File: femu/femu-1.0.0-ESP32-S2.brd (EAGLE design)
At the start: 24.1 x 15.8 mm, 44 parts

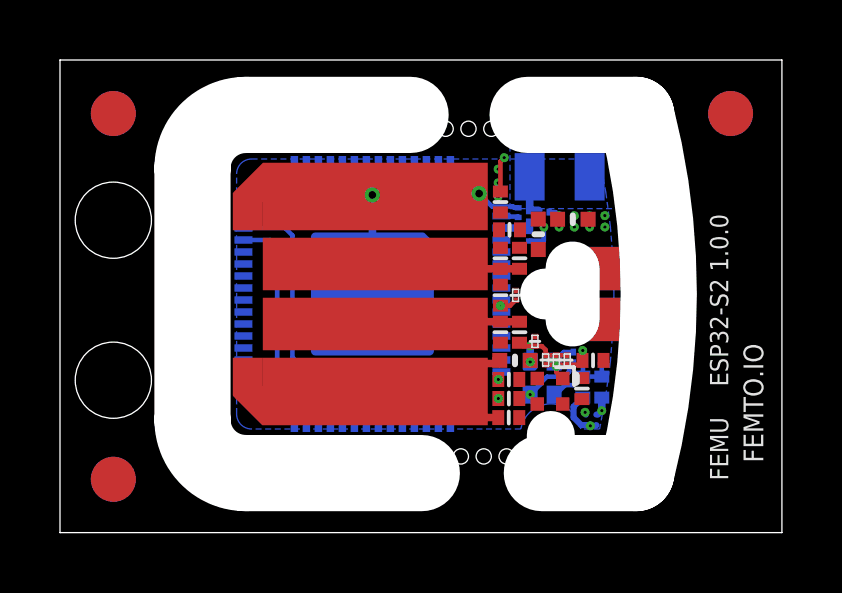
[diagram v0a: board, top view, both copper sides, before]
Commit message: Adding current work on FEMU v1.0.3, which includes microvia adjustments
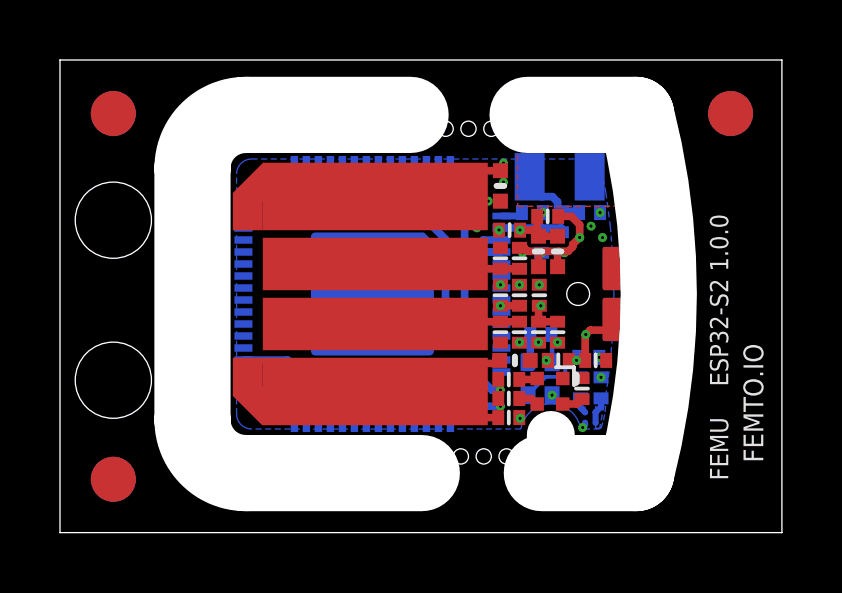
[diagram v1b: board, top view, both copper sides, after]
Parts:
- added FB2: (no value), microbuilder:_0402MP
- C12, C13, C16, C17, C19, C22, C4, C5, C8, C9, L2: device parts_01005:01005 -> parts_0201:PART
- moved C12 4.19 mm to (16.3, 10.5), turned to 180 degrees
- moved C18 3.37 mm to (16.0, 7.91)
- moved C9 1.51 mm to (17.7, 10.7)
- moved U$6 1.40 mm to (19.3, 7.95)
- moved C5 1.37 mm to (16.0, 6.60), turned to 180 degrees
- moved C11 1.19 mm to (16.6, 9.37), turned to 90 degrees
- moved C17 1.10 mm to (16.0, 6.68)
- moved C8 1.08 mm to (16.7, 10.4)
- moved C19 1.01 mm to (16.6, 6.68)
- moved C3 0.71 mm to (17.3, 4.83)
- moved C2 0.61 mm to (18.0, 4.83)
- moved C10 0.57 mm to (16.0, 9.37)
- moved C13 0.48 mm to (15.7, 10.7), turned to 0 degrees
- moved L2 0.45 mm to (16.1, 9.68)
- moved C4 0.40 mm to (17.6, 5.84)
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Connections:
- new net N$1: FB2.1, U$37.1/GND
- net GND: now also FB2.2; no longer U$37.1/GND
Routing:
- net 3.3V: track 28.1 -> 62.2 mm, vias 11 -> 16
- net GND: track 40.3 -> 7.05 mm, vias 19 -> 33
- net XIN: track 19.4 -> 2.35 mm, vias 4 -> 0
- net G: track 13.1 -> 0.00 mm, vias 3 -> 0
- net B: track 13.0 -> 0.00 mm, vias 3 -> 0
- net XOUT: track 10.4 -> 0.96 mm, vias 4 -> 0
- net N$13: track 0.00 -> 5.80 mm, vias 0 -> 3
- net N$1: track 0.00 -> 4.53 mm
- net VIN: track 4.80 -> 0.89 mm, vias 3 -> 0
- net N$5: track 8.36 -> 6.67 mm
- net N$6: track 1.60 -> 2.41 mm
- net ANT: track 1.48 -> 2.27 mm
- net R_: track 0.00 -> 0.71 mm
- net G_: track 0.00 -> 0.67 mm
- net B_: track 0.00 -> 0.61 mm
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- added copper zone on layer 16, net 3.3V
- added copper zone on layer 1, net GND
- added copper zone on layer 2, net GND
- added copper zone on layer 16, net VIN
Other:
- outline, holes or cut-outs redrawn
